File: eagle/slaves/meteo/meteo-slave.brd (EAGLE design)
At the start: 49.5 x 49.5 mm, 36 parts, among them CON1 SPI, IC1 MCP1703CB, J2 RJ12RIGHTANGLE-I2C, J3 RJ12RIGHTANGLE-I2C, U1 ATMEGA328P_TQFP, X1 8MHz, X2 1503_09, X3 1503_09

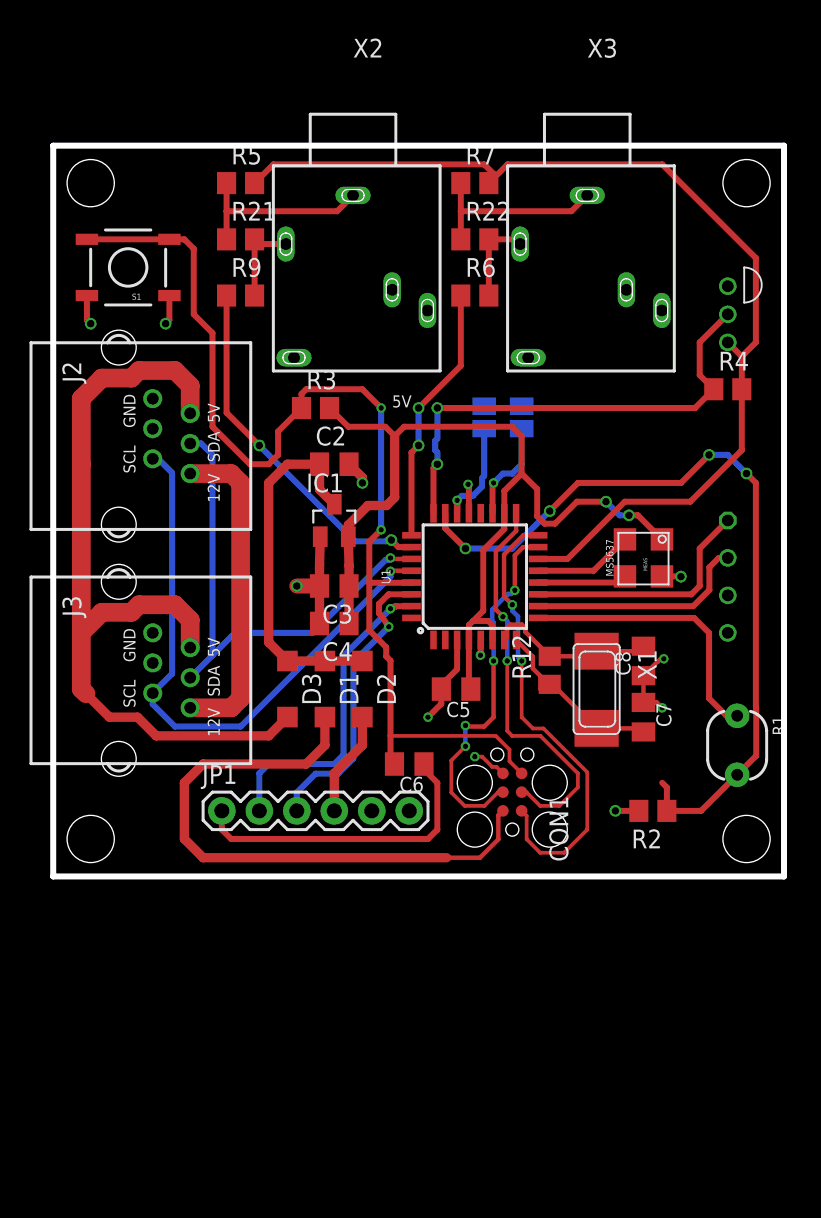
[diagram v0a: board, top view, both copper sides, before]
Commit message: meteo-slave: add voltage monitoring of i2c
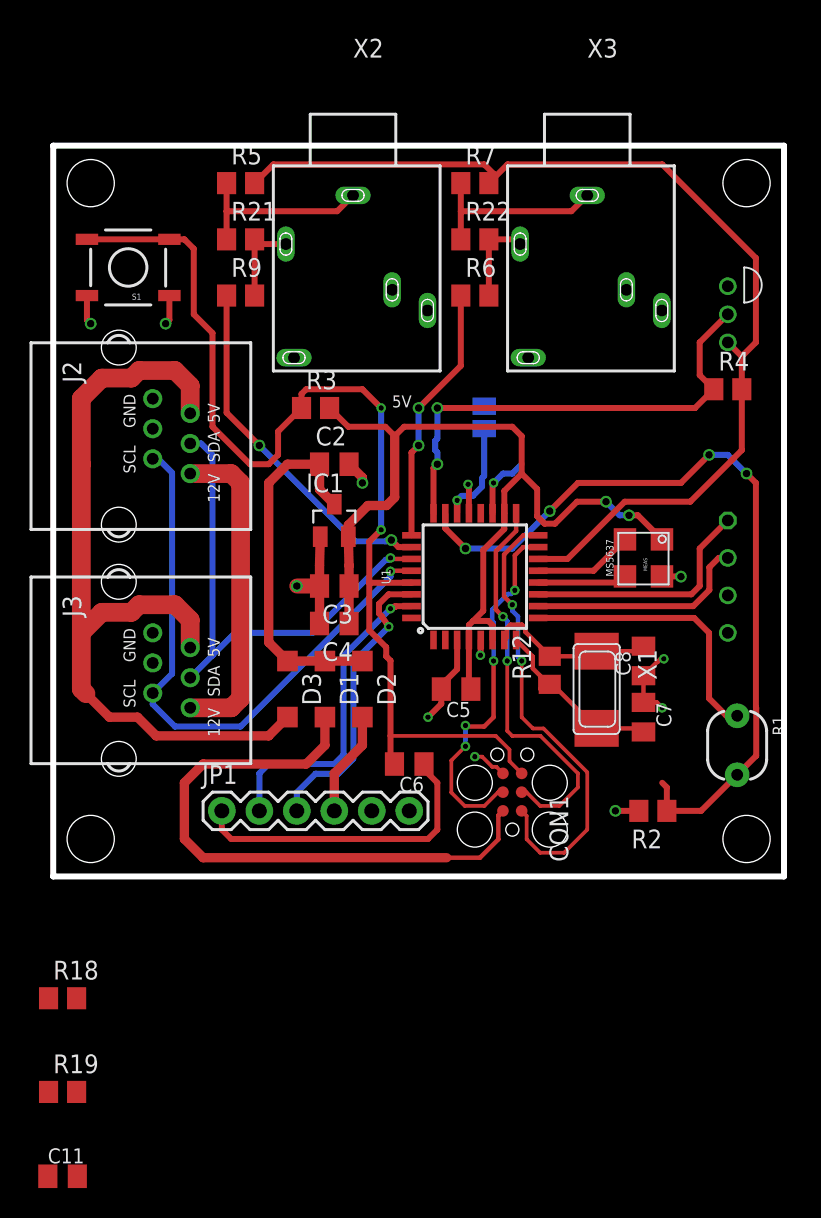
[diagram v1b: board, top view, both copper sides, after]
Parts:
- removed SJ1: A0, jumper:SJ
- added C11: 100nF, rcl:C0805K
- added R18: 1M, rcl:R0805
- added R19: 100k, rcl:R0805
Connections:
- net +5V: now also R18.2
- net A6: now also C11.2, R18.1, R19.2; no longer SJ1.1
- net GND: now also C11.1, R19.1; no longer SJ1.2
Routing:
- net A6: track 6.93 -> 4.52 mm
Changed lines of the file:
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@@
 <attribute name="VALUE" x="13.74645" y="14.65725" size="1.016" layer="27" rot="R270"/>
-</element>
-<element name="SJ1" library="jumper" library_urn="urn:adsk.eagle:library:252" package="SJ" package3d_urn="urn:adsk.eagle:package:15471/1" value="A0" x="31.75" y="31.115" smashed="yes" rot="MR90">
-<attribute name="NAME" x="32.893" y="29.464" size="1.27" layer="26" ratio="10" rot="MR90"/>
-<attribute name="VALUE" x="31.75" y="31.5151" size="0.02" layer="28" rot="MR90"/>
 </element>
 <element name="SJ2" library="jumper" library_urn="urn:adsk.eagle:library:252" package="SJ" package3d_urn="urn:adsk.eagle:package:15471/1" value="A1" x="29.21" y="31.115" smashed="yes" rot="MR90">
@@
 <attribute name="NAME" x="27.94" y="48.26" size="1.27" layer="25"/>
 <attribute name="VALUE" x="27.305" y="44.45" size="1.27" layer="27"/>
+</element>
+<element name="R18" library="rcl" package="R0805" value="1M" x="0.635" y="-8.255">
+<attribute name="ELECROW" value="C17514" x="0.635" y="-8.255" size="1.778" layer="27" display="off"/>
+<attribute name="LCSC" value="C17514" x="0.635" y="-8.255" size="1.778" layer="27" display="off"/>
+</element>
+<element name="R19" library="rcl" package="R0805" value="100k" x="0.635" y="-14.605">
+<attribute name="ELECROW" value="C17514" x="0.635" y="-14.605" size="1.778" layer="27" display="off"/>
+<attribute name="LCSC" value="C17514" x="0.635" y="-14.605" size="1.778" layer="27" display="off"/>
+</element>
+<element name="C11" library="rcl" library_urn="urn:adsk.eagle:library:334" package="C0805K" package3d_urn="urn:adsk.eagle:package:23681/2" value="100nF" x="0.635" y="-20.32">
+<attribute name="ELECROW" value="C49678" x="0.635" y="-20.32" size="1.778" layer="27" display="off"/>
+<attribute name="LCSC" value="C49678" x="0.635" y="-20.32" size="1.778" layer="27" display="off"/>
+<attribute name="MPN" value="80-C1206C104K5R" x="0.635" y="-20.32" size="1.778" layer="27" display="off"/>
 </element>
 </elements>
@@
 <wire x1="20.955" y1="27.035" x2="20.955" y2="26.67" width="0.635" layer="1"/>
 <via x="20.955" y="26.67" extent="1-16" drill="0.5"/>
-<contactref element="SJ1" pad="2"/>
 <contactref element="SJ2" pad="2"/>
 <contactref element="C8" pad="1"/>
@@
 <wire x1="2.286" y1="37.719" x2="2.54" y2="37.465" width="0.4064" layer="1"/>
 <via x="2.54" y="37.465" extent="1-16" drill="0.5"/>
+<contactref element="R19" pad="1"/>
+<contactref element="C11" pad="1"/>
 <wire x1="41.245" y1="38.36" x2="45.72" y2="40.005" width="0" layer="19" extent="1-1"/>
-<wire x1="31.75" y1="31.877" x2="41.245" y2="38.36" width="0" layer="19" extent="16-16"/>
-<wire x1="29.21" y1="31.877" x2="31.75" y2="31.877" width="0" layer="19" extent="16-16"/>
+<wire x1="29.21" y1="31.877" x2="41.245" y2="38.36" width="0" layer="19" extent="16-16"/>
 <wire x1="28.1178" y1="26.57475" x2="29.21" y2="31.877" width="0" layer="19" extent="16-16"/>
 <wire x1="20.955" y1="26.67" x2="28.1178" y2="26.57475" width="0" layer="19" extent="1-1"/>
 <wire x1="18.1" y1="23.03" x2="20.955" y2="26.67" width="0" layer="19" extent="1-1"/>
+<wire x1="25.37" y1="38.36" x2="29.21" y2="31.877" width="0" layer="19" extent="16-16"/>
 <wire x1="28.975" y1="16.0274" x2="28.175" y2="24.6126" width="0" layer="19" extent="1-1"/>
 <wire x1="27.375" y1="16.0274" x2="28.975" y2="16.0274" width="0" layer="19" extent="1-1"/>
@@
 <wire x1="45.72" y1="16.51" x2="41.3824" y2="14.7506" width="0" layer="19" extent="1-1"/>
 <wire x1="42.545" y1="20.32" x2="45.72" y2="16.51" width="0" layer="19" extent="1-1"/>
-<wire x1="25.37" y1="38.36" x2="29.21" y2="31.877" width="0" layer="19" extent="16-16"/>
 <wire x1="6.745" y1="16.51" x2="16.51" y2="19.685" width="0" layer="19" extent="1-1"/>
 <wire x1="6.745" y1="14.47" x2="6.745" y2="16.51" width="0" layer="19" extent="1-1"/>
@@
 <wire x1="7.62" y1="37.465" x2="6.745" y2="32.385" width="0" layer="19" extent="1-1"/>
 <wire x1="2.54" y1="37.465" x2="7.62" y2="37.465" width="0" layer="19" extent="1-1"/>
+<wire x1="-0.315" y1="-14.605" x2="21.59" y2="4.445" width="0" layer="19" extent="1-1"/>
+<wire x1="-0.365" y1="-20.32" x2="-0.315" y2="-14.605" width="0" layer="19" extent="1-1"/>
 </signal>
 <signal name="SCK">
@@
 <wire x1="6.98" y1="9.53" x2="14.605" y2="9.53" width="0.635" layer="1"/>
 <wire x1="14.605" y1="9.53" x2="15.875" y2="10.8" width="0.635" layer="1"/>
+<contactref element="R18" pad="2"/>
+<wire x1="1.585" y1="-8.255" x2="6.98" y2="9.53" width="0" layer="19" extent="1-1"/>
 </signal>
 <signal name="A3">
@@
 <signal name="A6">
 <contactref element="U1" pad="19"/>
-<contactref element="SJ1" pad="1"/>
 <wire x1="29.775" y1="24.6126" x2="29.775" y2="26.6" width="0.4064" layer="1"/>
 <wire x1="29.775" y1="26.6" x2="29.845" y2="26.67" width="0.4064" layer="1"/>
@@
 <wire x1="30.48" y1="27.305" x2="31.115" y2="27.305" width="0.4064" layer="16"/>
 <wire x1="31.115" y1="27.305" x2="31.75" y2="27.94" width="0.4064" layer="16"/>
-<wire x1="31.75" y1="27.94" x2="31.75" y2="30.353" width="0.4064" layer="16"/>
+<contactref element="R18" pad="1"/>
+<contactref element="R19" pad="2"/>
+<contactref element="C11" pad="2"/>
+<wire x1="-0.315" y1="-8.255" x2="29.775" y2="24.6126" width="0" layer="19" extent="1-1"/>
+<wire x1="1.585" y1="-14.605" x2="-0.315" y2="-8.255" width="0" layer="19" extent="1-1"/>
+<wire x1="1.635" y1="-20.32" x2="1.585" y2="-14.605" width="0" layer="19" extent="1-1"/>
 </signal>
 <signal name="A7">
